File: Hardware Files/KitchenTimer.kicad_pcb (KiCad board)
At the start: 2 copper layers, 100 x 100 mm, 0 parts

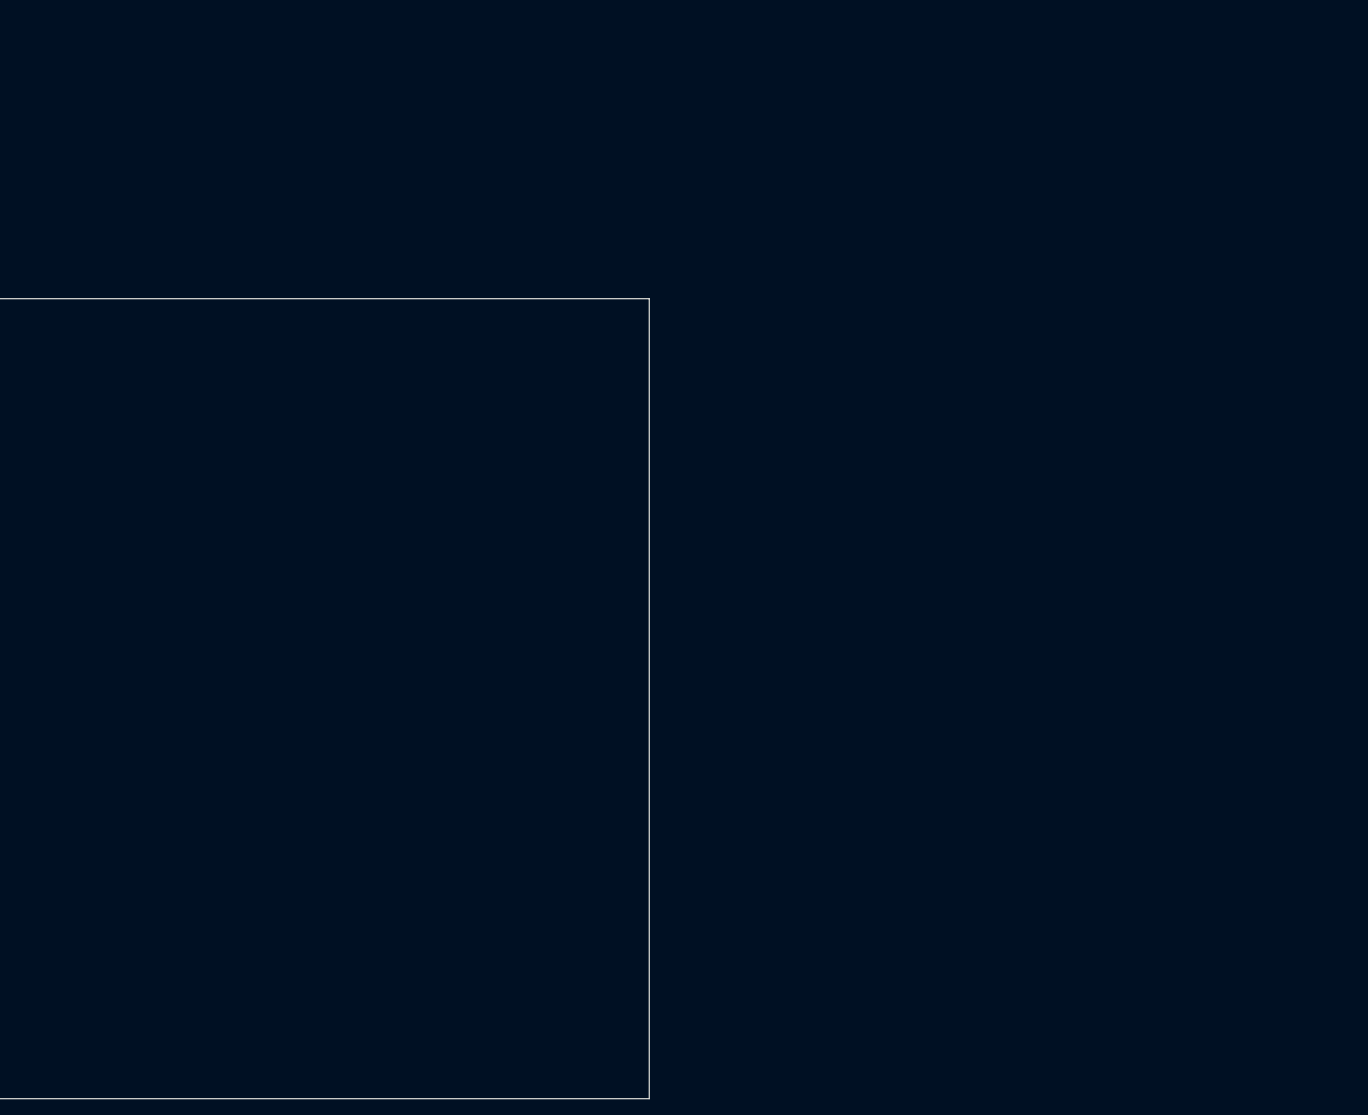
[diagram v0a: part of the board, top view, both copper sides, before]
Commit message: push components to PCB
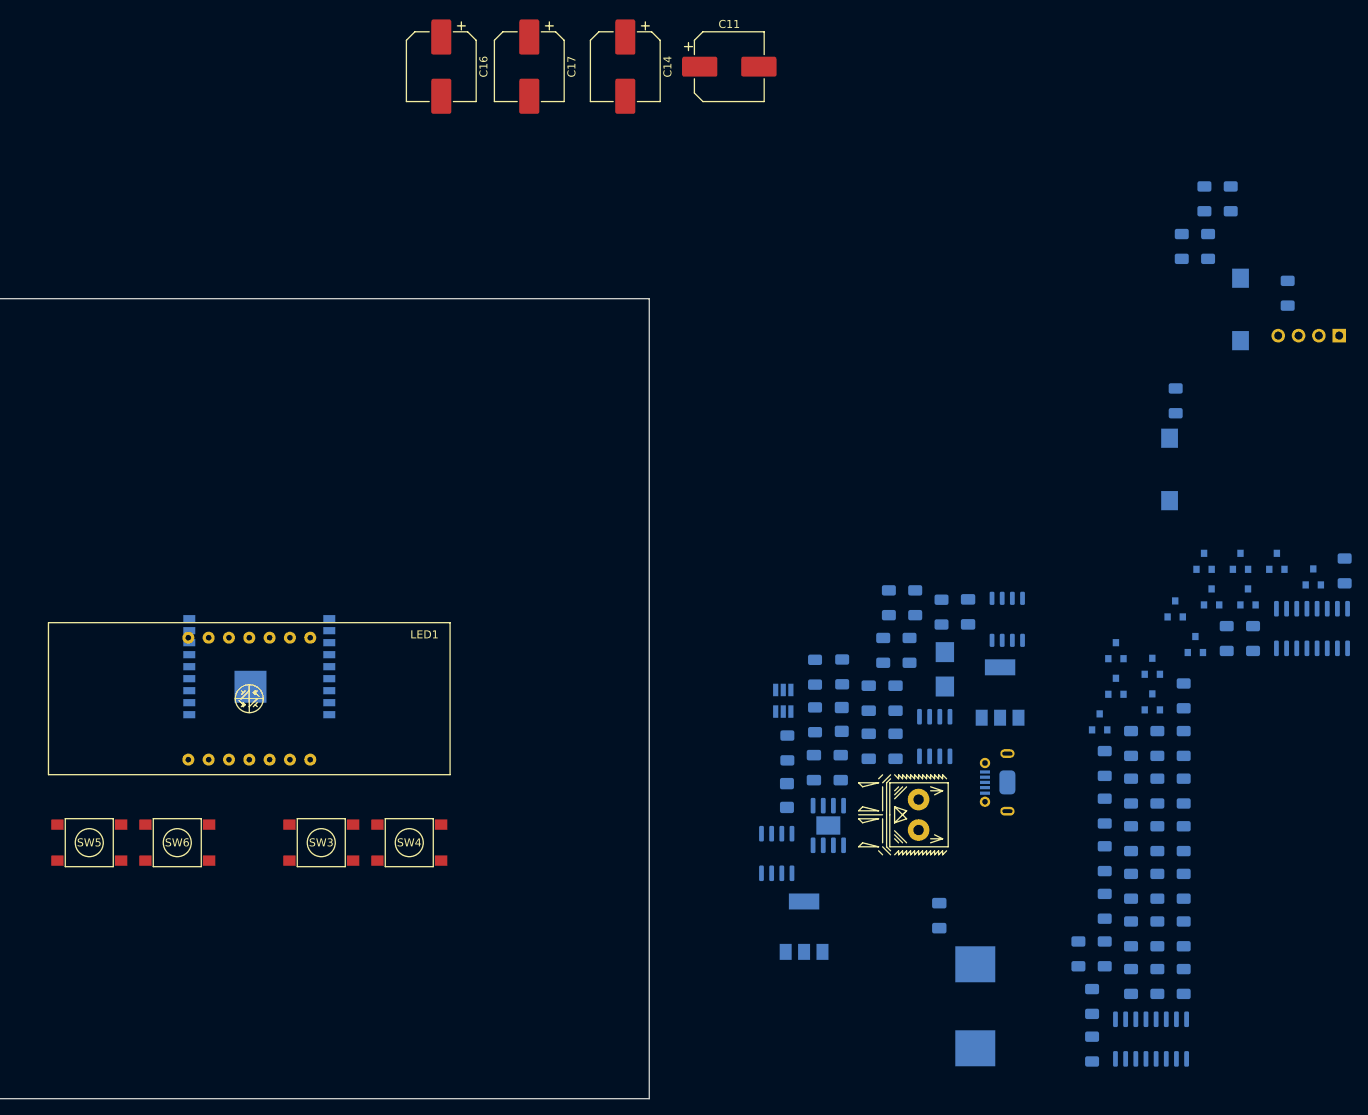
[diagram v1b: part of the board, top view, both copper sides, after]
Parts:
- added C11: 100uF ±20% 50V, Capacitor_SMD:CP_Elec_8x10.5, F.Cu at (110.0, -29.0)
- added C12: 10uF ±10% 25V X5R, Capacitor_SMD:C_1206_3216Metric_Pad1.33x1.80mm_HandSolder, B.Cu at (139.8, 39.1)
- added C13: NP0 500V ±5% 100pF 1206, Capacitor_SMD:C_1206_3216Metric_Pad1.33x1.80mm_HandSolder, B.Cu at (130.8, 49.9)
- added C14: 100uF ±20% 50V, Capacitor_SMD:CP_Elec_8x10.5, F.Cu at (97.0, -29.0)
- added C15: 10uF ±10% 25V X5R, Capacitor_SMD:C_1206_3216Metric_Pad1.33x1.80mm_HandSolder, B.Cu at (120.6, 58.6)
- added C16: 100uF ±20% 50V, Capacitor_SMD:CP_Elec_8x10.5, F.Cu at (74.0, -29.0)
- added C17: 100uF ±20% 50V, Capacitor_SMD:CP_Elec_8x10.5, F.Cu at (85.0, -29.0)
- added C18: 100nF ±10% 50V X7R, Capacitor_SMD:C_1206_3216Metric_Pad1.33x1.80mm_HandSolder, B.Cu at (123.9, 58.6)
- added C19: 220nF 50V, Capacitor_SMD:C_1206_3216Metric_Pad1.33x1.80mm_HandSolder, B.Cu at (130.8, 56.0)
- added C20: 220nF 50V, Capacitor_SMD:C_1206_3216Metric_Pad1.33x1.80mm_HandSolder, B.Cu at (127.4, 56.0)
- added C21: 220nF 50V, Capacitor_SMD:C_1206_3216Metric_Pad1.33x1.80mm_HandSolder, B.Cu at (136.2, 77.1)
- added C22: 220nF 50V, Capacitor_SMD:C_1206_3216Metric_Pad1.33x1.80mm_HandSolder, B.Cu at (127.4, 49.9)
- added D1: Orange LED, Diode_SMD:D_1206_3216Metric_Pad1.42x1.75mm_HandSolder, B.Cu at (117.2, 62.1)
- added D2: Green LED, Diode_SMD:D_1206_3216Metric_Pad1.42x1.75mm_HandSolder, B.Cu at (124.1, 52.6)
- added D3: 40V 3A 500mV@3A, Diode_SMD:D_SMB, B.Cu at (136.9, 46.3)
- added J1: Conn_01x04, Connector_PinHeader_2.54mm:PinHeader_1x04_P2.54mm_Vertical, B.Cu at (186.2, 4.62)
- added J2: USB_B_Micro, .[--Stasis.Footprints.Library:U-F-M5DD-Y-L, B.Cu at (142.0, 60.5)
- added J3: Battery, .[--Stasis.Footprints.Library:WJ124-3.81-2P, B.Cu at (133.7, 64.5)
- added L1: 100µH 20% 1A, Inductor_SMD:L_Wuerth_HCI-1350, B.Cu at (140.8, 88.5)
- added LED1: SLR0564DBA4BD, KitchenTimer:SLR0564DBA4BD, F.Cu at (50.0, 50.0)
- added Q1: P 1V 250uA 4A SOT-23, Package_TO_SOT_SMD:SOT-23, B.Cu at (158.3, 48.5)
- added Q10: Q_NMOS_GSD, Package_TO_SOT_SMD:SOT-23, B.Cu at (168.3, 43.2)
- added Q11: Q_NMOS_GSD, Package_TO_SOT_SMD:SOT-23, B.Cu at (165.7, 38.8)
- added Q12: Q_NMOS_GSD, Package_TO_SOT_SMD:SOT-23, B.Cu at (169.3, 32.8)
- added Q13: Q_NMOS_GSD, Package_TO_SOT_SMD:SOT-23, B.Cu at (158.3, 44.0)
- added Q14: -30V 12A 14mΩ @ 8A, .[--Stasis.Footprints.Library:SOP-8_3.9x4.9mm_P1.27mm, B.Cu at (144.8, 40.1)
- added Q15: 20V 7.5A 24mΩ @ 2.5Vgs, Package_SO:SOIC-8_3.9x4.9mm_P1.27mm, B.Cu at (115.9, 69.3)
- added Q2: P 1V 250uA 4A SOT-23, Package_TO_SOT_SMD:SOT-23, B.Cu at (173.9, 32.8)
- added Q3: P 1V 250uA 4A SOT-23, Package_TO_SOT_SMD:SOT-23, B.Cu at (178.4, 32.8)
- added Q4: P 1V 250uA 4A SOT-23, Package_TO_SOT_SMD:SOT-23, B.Cu at (162.9, 46.0)
- added Q5: P 1V 250uA 4A SOT-23, Package_TO_SOT_SMD:SOT-23, B.Cu at (174.8, 37.3)
- added Q6: Q_NMOS_GSD, Package_TO_SOT_SMD:SOT-23, B.Cu at (183.0, 34.8)
- added Q7: Q_NMOS_GSD, Package_TO_SOT_SMD:SOT-23, B.Cu at (162.9, 50.4)
- added Q8: Q_NMOS_GSD, Package_TO_SOT_SMD:SOT-23, B.Cu at (156.3, 52.9)
- added Q9: Q_NMOS_GSD, Package_TO_SOT_SMD:SOT-23, B.Cu at (170.3, 37.3)
- added R1: R, Resistor_SMD:R_1206_3216Metric_Pad1.30x1.75mm_HandSolder, B.Cu at (166.8, 61.5)
- added R10: R, Resistor_SMD:R_1206_3216Metric_Pad1.30x1.75mm_HandSolder, B.Cu at (156.9, 70.0)
- added R11: R, Resistor_SMD:R_1206_3216Metric_Pad1.30x1.75mm_HandSolder, B.Cu at (156.9, 64.0)
- added R12: R, Resistor_SMD:R_1206_3216Metric_Pad1.30x1.75mm_HandSolder, B.Cu at (156.9, 58.1)
- added R13: R, Resistor_SMD:R_1206_3216Metric_Pad1.30x1.75mm_HandSolder, B.Cu at (155.3, 93.8)
- added R14: R, Resistor_SMD:R_1206_3216Metric_Pad1.30x1.75mm_HandSolder, B.Cu at (160.2, 73.5)
- added R15: 0R, Resistor_SMD:R_1206_3216Metric_Pad1.30x1.75mm_HandSolder, B.Cu at (166.8, 85.3)
- added R16: 0R, Resistor_SMD:R_1206_3216Metric_Pad1.30x1.75mm_HandSolder, B.Cu at (175.5, 42.5)
- added R17: 10k, Resistor_SMD:R_1206_3216Metric_Pad1.30x1.75mm_HandSolder, B.Cu at (155.3, 87.8)
- added R18: 10k, Resistor_SMD:R_1206_3216Metric_Pad1.30x1.75mm_HandSolder, B.Cu at (166.8, 79.4)
- added R19: 10k, Resistor_SMD:R_1206_3216Metric_Pad1.30x1.75mm_HandSolder, B.Cu at (163.5, 85.3)
- added R2: R, Resistor_SMD:R_1206_3216Metric_Pad1.30x1.75mm_HandSolder, B.Cu at (166.8, 55.6)
- added R20: 10k, Resistor_SMD:R_1206_3216Metric_Pad1.30x1.75mm_HandSolder, B.Cu at (186.9, 34.0)
- added R21: 10k, Resistor_SMD:R_1206_3216Metric_Pad1.30x1.75mm_HandSolder, B.Cu at (163.5, 79.4)
- added R22: 10k, Resistor_SMD:R_1206_3216Metric_Pad1.30x1.75mm_HandSolder, B.Cu at (160.2, 85.3)
- added R23: 10k, Resistor_SMD:R_1206_3216Metric_Pad1.30x1.75mm_HandSolder, B.Cu at (166.8, 73.5)
- added R24: 10k, Resistor_SMD:R_1206_3216Metric_Pad1.30x1.75mm_HandSolder, B.Cu at (156.9, 81.9)
- added R25: 10k, Resistor_SMD:R_1206_3216Metric_Pad1.30x1.75mm_HandSolder, B.Cu at (160.2, 79.4)
- added R26: 10k, Resistor_SMD:R_1206_3216Metric_Pad1.30x1.75mm_HandSolder, B.Cu at (172.2, 42.5)
- added R27: 10k, Resistor_SMD:R_1206_3216Metric_Pad1.30x1.75mm_HandSolder, B.Cu at (163.5, 73.5)
- added R28: 10k, Resistor_SMD:R_1206_3216Metric_Pad1.30x1.75mm_HandSolder, B.Cu at (156.9, 76.0)
- added R29: 10k, Resistor_SMD:R_1206_3216Metric_Pad1.30x1.75mm_HandSolder, B.Cu at (166.8, 67.5)
- added R3: R, Resistor_SMD:R_1206_3216Metric_Pad1.30x1.75mm_HandSolder, B.Cu at (166.8, 49.6)
- added R30: 10k, Resistor_SMD:R_1206_3216Metric_Pad1.30x1.75mm_HandSolder, B.Cu at (153.6, 81.9)
- added R31: 10k, Resistor_SMD:R_1206_3216Metric_Pad1.30x1.75mm_HandSolder, B.Cu at (169.4, -12.5)
- added R32: 10k, Resistor_SMD:R_1206_3216Metric_Pad1.30x1.75mm_HandSolder, B.Cu at (172.7, -12.5)
- added R33: 10k, Resistor_SMD:R_1206_3216Metric_Pad1.30x1.75mm_HandSolder, B.Cu at (166.6, -6.53)
- added R34: 10k, Resistor_SMD:R_1206_3216Metric_Pad1.30x1.75mm_HandSolder, B.Cu at (169.8, -6.53)
- added R35: 10k, Resistor_SMD:R_1206_3216Metric_Pad1.30x1.75mm_HandSolder, B.Cu at (179.8, -0.68)
- added R36: 10k, Resistor_SMD:R_1206_3216Metric_Pad1.30x1.75mm_HandSolder, B.Cu at (165.8, 12.8)
- added R37: 0.3R, Resistor_SMD:R_1206_3216Metric_Pad1.30x1.75mm_HandSolder, B.Cu at (117.3, 56.2)
- added R38: 10k, Resistor_SMD:R_1206_3216Metric_Pad1.30x1.75mm_HandSolder, B.Cu at (136.5, 39.2)
- added R39: 10k, Resistor_SMD:R_1206_3216Metric_Pad1.30x1.75mm_HandSolder, B.Cu at (120.7, 52.6)
- added R4: R, Resistor_SMD:R_1206_3216Metric_Pad1.30x1.75mm_HandSolder, B.Cu at (163.5, 67.5)
- added R40: 180R, Resistor_SMD:R_1206_3216Metric_Pad1.30x1.75mm_HandSolder, B.Cu at (129.9, 38.0)
- added R41: 1.2kΩ ±1% 0.25W, Resistor_SMD:R_1206_3216Metric_Pad1.30x1.75mm_HandSolder, B.Cu at (120.7, 46.7)
- added R42: 200k, Resistor_SMD:R_1206_3216Metric_Pad1.30x1.75mm_HandSolder, B.Cu at (133.2, 38.0)
- added R43: 47k, Resistor_SMD:R_1206_3216Metric_Pad1.30x1.75mm_HandSolder, B.Cu at (124.1, 46.6)
- added R44: 330R ±1% 0.25W, Resistor_SMD:R_1206_3216Metric_Pad1.30x1.75mm_HandSolder, B.Cu at (129.2, 44.0)
- added R45: 1.2kΩ ±1% 0.25W, Resistor_SMD:R_1206_3216Metric_Pad1.30x1.75mm_HandSolder, B.Cu at (132.5, 44.0)
- added R5: R, Resistor_SMD:R_1206_3216Metric_Pad1.30x1.75mm_HandSolder, B.Cu at (163.5, 61.5)
- added R6: R, Resistor_SMD:R_1206_3216Metric_Pad1.30x1.75mm_HandSolder, B.Cu at (163.5, 55.6)
- added R7: R, Resistor_SMD:R_1206_3216Metric_Pad1.30x1.75mm_HandSolder, B.Cu at (160.2, 67.5)
- added R8: R, Resistor_SMD:R_1206_3216Metric_Pad1.30x1.75mm_HandSolder, B.Cu at (160.2, 61.5)
- added R9: R, Resistor_SMD:R_1206_3216Metric_Pad1.30x1.75mm_HandSolder, B.Cu at (160.2, 55.6)
- added SW1: SW_SPST, .[--Stasis.Footprints.Library:PTS636_SM25F_SMTR_LFS, B.Cu at (173.9, 5.25)
- added SW2: SW_SPST, .[--Stasis.Footprints.Library:PTS636_SM25F_SMTR_LFS, B.Cu at (165.0, 25.2)
- added SW3: SW_Push_Dual, .[--Stasis.Footprints.Library:PTS645SK50SMTR92LFS, F.Cu at (59.0, 68.0)
- added SW4: SW_Push_Dual, .[--Stasis.Footprints.Library:PTS645SK50SMTR92LFS, F.Cu at (70.0, 68.0)
- added SW5: SW_Push_Dual, .[--Stasis.Footprints.Library:PTS645SK50SMTR92LFS, F.Cu at (30.0, 68.0)
- added SW6: SW_Push_Dual, .[--Stasis.Footprints.Library:PTS645SK50SMTR92LFS, F.Cu at (41.0, 68.0)
- added U1: 74HC595, Package_SO:SOIC-16_3.9x9.9mm_P1.27mm, B.Cu at (182.8, 41.2)
- added U2: 74HC595, Package_SO:SOIC-16_3.9x9.9mm_P1.27mm, B.Cu at (162.7, 92.5)
- added U3: ESP-WROOM-02D, .[--Stasis.Footprints.Library:ESP-WROOM-02D, B.Cu at (60.0, 40.0)
- added U4: AP34063S8G-13, Package_SO:SOIC-8_3.9x4.9mm_P1.27mm, B.Cu at (135.7, 54.7)
- added U5: TP4056, .[--Stasis.Footprints.Library:SOIC-8-1EP_3.9x4.9mm_P1.27mm_EP2.29x3mm, B.Cu at (122.4, 65.8)
- added U6: AP9101CK6, Package_TO_SOT_SMD:SOT-23-6_Handsoldering, B.Cu at (116.8, 50.3)
- added U7: NCP1117ST50T3G, Package_TO_SOT_SMD:SOT-223-3_TabPin2, B.Cu at (143.8, 49.2)
- added U8: NCP1117ST33T3G, Package_TO_SOT_SMD:SOT-223-3_TabPin2, B.Cu at (119.3, 78.5)

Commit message: remove current limit resistors to each char
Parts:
- removed R1, R2, R3, R4, R5: R, Resistor_SMD:R_1206_3216Metric_Pad1.30x1.75mm_HandSolder
- moved U3 160.4 mm to (211.0, -14.0)
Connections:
- LED1 pad 10: Net-(LED1-Pad10) -> Char_3_Power
- LED1 pad 11: Net-(LED1-Pad11) -> Char_2_Power
- LED1 pad 14: Net-(LED1-Pad14) -> Char_1_Power
- LED1 pad 6: Net-(LED1-Pad6) -> Char_4_Power
- LED1 pad 7: Net-(LED1-Pad7) -> Char_(':')_Power

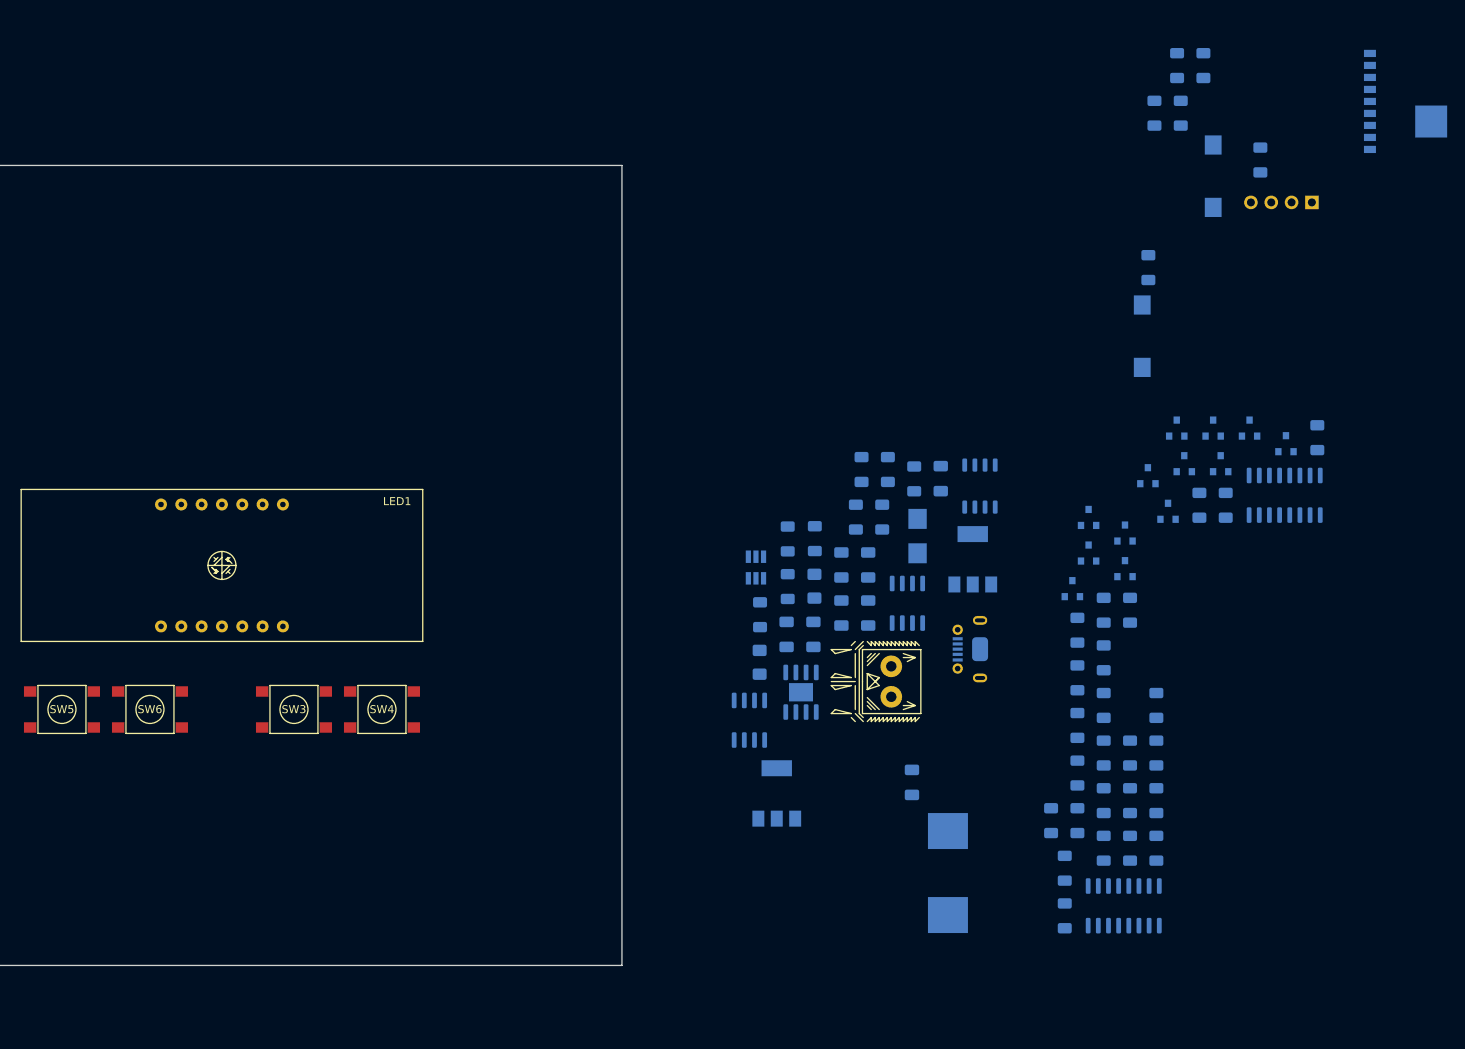
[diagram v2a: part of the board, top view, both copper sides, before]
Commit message: change resistors to 0805
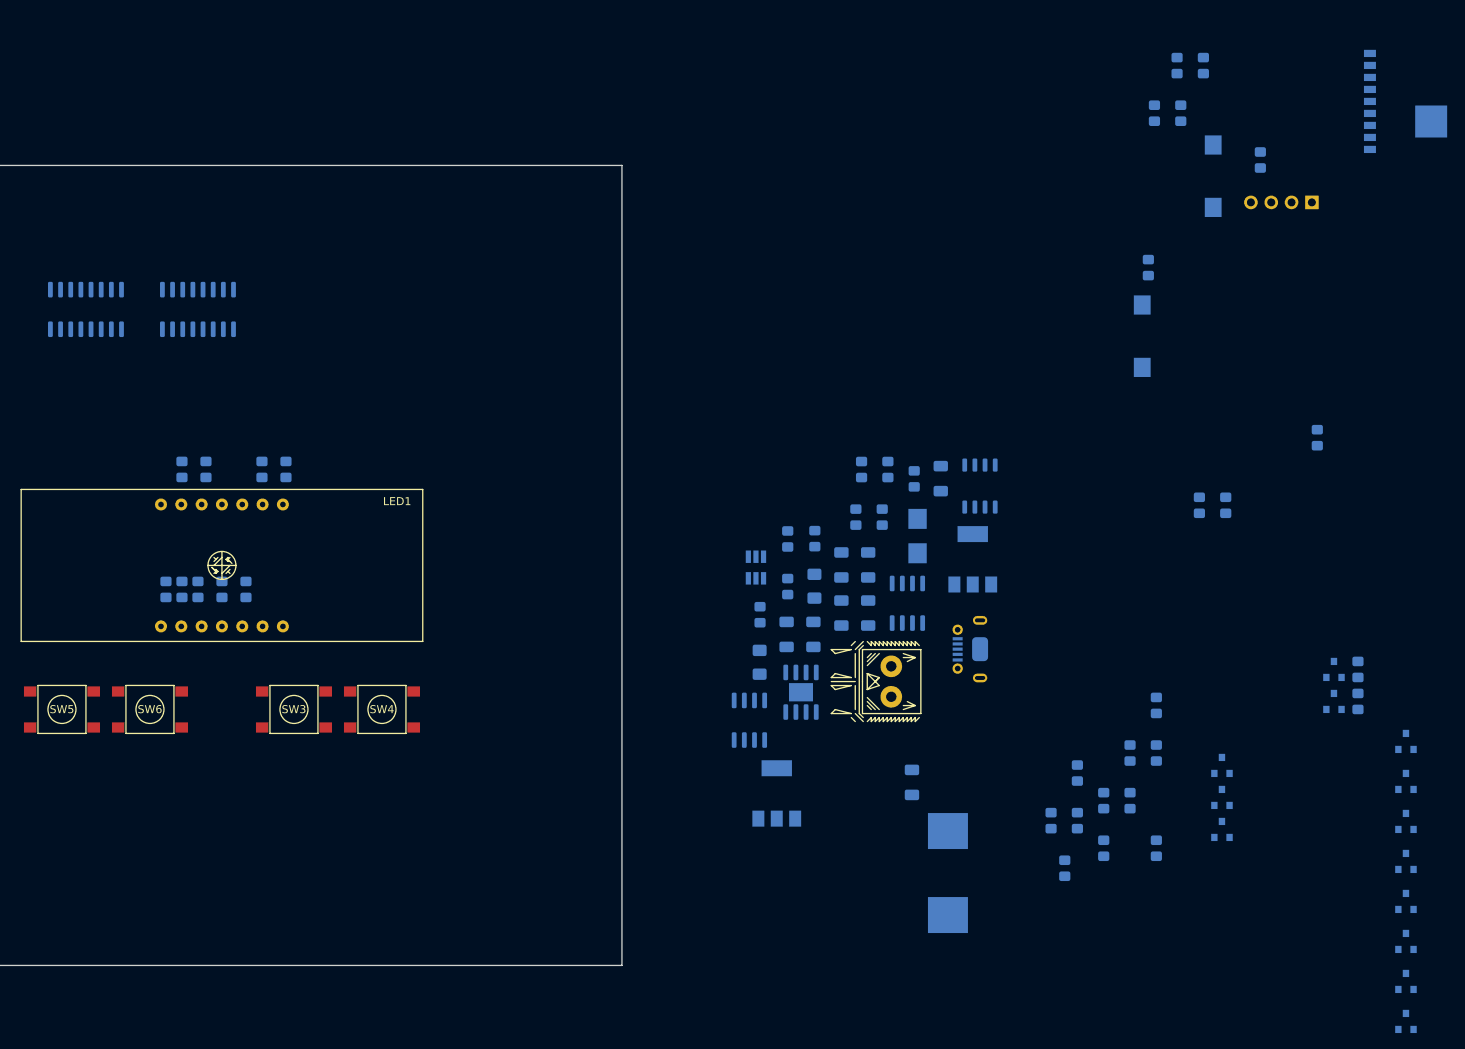
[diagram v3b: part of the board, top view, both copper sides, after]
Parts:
- R10, R11, R12, R13, R14, R15, R16, R17, R18, R19, R20, R21, R22, R23, R24, R25, R26, R27, R28, R29, R30, R31, R32, R33, R34, R35, R36, R37, R38, R39, R40, R41, R42, R43, R44, R45, R6, R7, R8, R9: footprint Resistor_SMD:R_1206_3216Metric_Pad1.30x1.75mm_HandSolder -> Resistor_SMD:R_0805_2012Metric_Pad1.20x1.40mm_HandSolder
- moved U2 149.6 mm to (33.0, 18.0)
- moved U1 137.8 mm to (47.0, 18.0)
- moved R6 119.8 mm to (45.0, 38.0)
- moved R13 115.8 mm to (47.0, 53.0)
- moved R9 115.2 mm to (45.0, 53.0)
- moved R10 115.2 mm to (43.0, 53.0)
- moved R11 112.0 mm to (48.0, 38.0), turned to 270 degrees
- moved R8 110.6 mm to (50.0, 53.0), turned to 270 degrees
- moved R7 109.3 mm to (55.0, 38.0)
- moved R14 108.2 mm to (58.0, 38.0)
- moved R12 104.1 mm to (53.0, 53.0)
- moved Q12 74.9 mm to (198.0, 102.0)
- moved Q13 74.4 mm to (198.0, 107.0)
- moved Q11 66.6 mm to (198.0, 97.0)
- moved Q10 57.1 mm to (198.0, 92.0)
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
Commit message: fix ground naming
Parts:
- moved R24 62.9 mm to (218.0, 67.0), turned to 270 degrees
- moved R25 58.3 mm to (218.0, 72.0), turned to 270 degrees
- moved R26 57.4 mm to (218.0, 77.0), turned to 270 degrees
- moved R27 55.2 mm to (218.0, 82.0), turned to 270 degrees
- moved R23 52.5 mm to (218.0, 62.0), turned to 270 degrees
- moved R20 38.3 mm to (192.0, 72.0)
- moved R22 32.0 mm to (192.0, 82.0)
- moved R21 28.6 mm to (192.0, 77.0)
- moved Q10 19.7 mm to (215.0, 82.0), turned to 180 degrees
- moved Q11 19.7 mm to (215.0, 87.0), turned to 180 degrees
- moved Q12 19.7 mm to (215.0, 92.0), turned to 180 degrees
- moved Q13 19.7 mm to (215.0, 97.0), turned to 180 degrees
- moved Q6 19.7 mm to (215.0, 62.0), turned to 180 degrees
- moved Q7 19.7 mm to (215.0, 67.0), turned to 180 degrees
- moved Q8 19.7 mm to (215.0, 72.0), turned to 180 degrees
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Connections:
- net LED_':'_Sink renamed GND
